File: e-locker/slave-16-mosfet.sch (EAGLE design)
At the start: 133 parts, among them IC1 PCF8574P, IC2 PCF8574P, IC3 PCF8574P, IC4 PCF8574P, Q1 BC547B, Q2 BC547B, Q3 BC547B, Q4 BC547B, Q5 BC547B, Q6 BC547B, Q7 BC547B, Q8 BC547B, T1 BC547, T2 BC547, T3 BC547, T4 BC547, T5 BC547, T6 BC547, T7 BC547, T8 BC547, X1 JST-XH-02-PIN-LONG-PAD, X10 JST-XH-04-PIN-LONG-PAD, X11 JST-XH-02-PIN-LONG-PAD, X12 JST-XH-04-PIN-LONG-PAD, X13 JST-XH-04-PIN-LONG-PAD, X14 JST-XH-04-PIN-LONG-PAD, X15 JST-XH-04-PIN-LONG-PAD, X16 JST-XH-04-PIN-LONG-PAD, X17 JST-XH-04-PIN-LONG-PAD, X18 JST-XH-04-PIN-LONG-PAD, X19 JST-XH-04-PIN-LONG-PAD, X2 JST-XH-05-PIN-LONG-PAD, X20 JST-XH-05-PIN-LONG-PAD, X21 JST-XH-02-PIN-LONG-PAD, X22 JST-XH-02-PIN-LONG-PAD, X3 JST-XH-04-PIN-LONG-PAD, X4 JST-XH-04-PIN-LONG-PAD, X5 JST-XH-04-PIN-LONG-PAD, X6 JST-XH-04-PIN-LONG-PAD, X7 JST-XH-04-PIN-LONG-PAD, X8 JST-XH-04-PIN-LONG-PAD, X9 JST-XH-04-PIN-LONG-PAD

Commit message: WIP
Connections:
- removed net N$11: R43.1, U$1.G
- new net N$81: R43.1, R59.2, U$1.G
- net N$12: now also R60.2
- net N$13: now also R61.2
- net N$14: now also R62.2
- net N$56: now also R66.2
- net N$59: now also R65.2
- net N$63: now also R64.2
- net N$64: now also R63.2
- net V24: no longer R59.2, R60.2, R61.2, R62.2, R63.2, R64.2, R65.2, R66.2
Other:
- moved on the sheet: R60, R61, R62, R63, R64, R65, R66

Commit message: new master and slave16 changes
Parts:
- removed JP2: (no value), pinhead-zmiany-JP:PINHD-2X8
- added JP3: (no value), adafruit:PINHD-2X4
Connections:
- net GND: now also JP3.2, JP3.4, JP3.6, JP3.8; no longer JP2.10, JP2.12, JP2.14, JP2.16, JP2.2, JP2.4, JP2.6, JP2.8
- net N$10: no longer JP2.15
- net N$17: no longer JP2.13
- net N$20: no longer JP2.11
- net N$21: no longer JP2.9
- net N$22: now also JP3.7; no longer JP2.7
- net N$23: now also JP3.5; no longer JP2.5
- net N$24: now also JP3.3; no longer JP2.3
- net N$25: now also JP3.1; no longer JP2.1
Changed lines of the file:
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@@
 <part name="X11" library="Rembrandt Electronics - JST XH Connectors v1-0" deviceset="JST-XH-02-PIN" device="-LONG-PAD"/>
 <part name="U$10" library="zort-library" deviceset="RS485-TTL-CONVERTER" device=""/>
-<part name="JP2" library="pinhead-zmiany-JP" deviceset="PINHD-2X8" device="" package3d_urn="urn:adsk.eagle:package:22481/2"/>
 <part name="IC1" library="micro-philips" library_urn="urn:adsk.eagle:library:290" deviceset="PCF8574" device="P" package3d_urn="urn:adsk.eagle:package:20171/1"/>
 <part name="IC2" library="micro-philips" library_urn="urn:adsk.eagle:library:290" deviceset="PCF8574" device="P" package3d_urn="urn:adsk.eagle:package:20171/1"/>
@@
 <part name="R65" library="eagle-ltspice" library_urn="urn:adsk.eagle:library:217" deviceset="R" device="R1206" package3d_urn="urn:adsk.eagle:package:13301/1"/>
 <part name="R66" library="eagle-ltspice" library_urn="urn:adsk.eagle:library:217" deviceset="R" device="R1206" package3d_urn="urn:adsk.eagle:package:13301/1"/>
+<part name="JP3" library="adafruit" library_urn="urn:adsk.eagle:library:420" deviceset="PINHD-2X4" device="" package3d_urn="urn:adsk.eagle:package:6240893/1"/>
 </parts>
 <sheets>
@@
 <attribute name="VALUE" x="205.74" y="91.44" size="1.778" layer="96"/>
 </instance>
-<instance part="JP2" gate="A" x="251.46" y="170.18" smashed="yes">
-<attribute name="NAME" x="245.11" y="180.975" size="1.778" layer="95"/>
-<attribute name="VALUE" x="245.11" y="154.94" size="1.778" layer="96"/>
-</instance>
 <instance part="IC1" gate="G$1" x="289.56" y="259.08" smashed="yes">
 <attribute name="NAME" x="281.94" y="275.59" size="1.778" layer="95"/>
@@
 <attribute name="NAME" x="361.95" y="146.2786" size="1.778" layer="95"/>
 <attribute name="VALUE" x="361.95" y="141.478" size="1.778" layer="96"/>
+</instance>
+<instance part="JP3" gate="A" x="251.46" y="172.72" smashed="yes">
+<attribute name="NAME" x="245.11" y="180.975" size="1.778" layer="95"/>
+<attribute name="VALUE" x="245.11" y="165.1" size="1.778" layer="96"/>
 </instance>
 </instances>
@@
 </segment>
 <segment>
-<pinref part="JP2" gate="A" pin="2"/>
 <wire x1="256.54" y1="177.8" x2="264.16" y2="177.8" width="0.1524" layer="91"/>
 <pinref part="GND3" gate="1" pin="GND"/>
 <wire x1="264.16" y1="177.8" x2="264.16" y2="175.26" width="0.1524" layer="91"/>
-<pinref part="JP2" gate="A" pin="4"/>
 <wire x1="264.16" y1="175.26" x2="264.16" y2="172.72" width="0.1524" layer="91"/>
 <wire x1="264.16" y1="172.72" x2="264.16" y2="170.18" width="0.1524" layer="91"/>
@@
 <wire x1="256.54" y1="175.26" x2="264.16" y2="175.26" width="0.1524" layer="91"/>
 <junction x="264.16" y="175.26"/>
-<pinref part="JP2" gate="A" pin="6"/>
 <wire x1="256.54" y1="172.72" x2="264.16" y2="172.72" width="0.1524" layer="91"/>
 <junction x="264.16" y="172.72"/>
-<pinref part="JP2" gate="A" pin="8"/>
 <wire x1="256.54" y1="170.18" x2="264.16" y2="170.18" width="0.1524" layer="91"/>
 <junction x="264.16" y="170.18"/>
-<pinref part="JP2" gate="A" pin="10"/>
 <wire x1="256.54" y1="167.64" x2="264.16" y2="167.64" width="0.1524" layer="91"/>
 <junction x="264.16" y="167.64"/>
-<pinref part="JP2" gate="A" pin="12"/>
 <wire x1="256.54" y1="165.1" x2="264.16" y2="165.1" width="0.1524" layer="91"/>
 <junction x="264.16" y="165.1"/>
-<pinref part="JP2" gate="A" pin="14"/>
 <wire x1="256.54" y1="162.56" x2="264.16" y2="162.56" width="0.1524" layer="91"/>
 <junction x="264.16" y="162.56"/>
-<pinref part="JP2" gate="A" pin="16"/>
 <wire x1="256.54" y1="160.02" x2="264.16" y2="160.02" width="0.1524" layer="91"/>
 <junction x="264.16" y="160.02"/>
@@
 <wire x1="243.84" y1="157.48" x2="264.16" y2="157.48" width="0.1524" layer="91"/>
 <junction x="264.16" y="157.48"/>
+<pinref part="JP3" gate="A" pin="2"/>
+<pinref part="JP3" gate="A" pin="4"/>
+<pinref part="JP3" gate="A" pin="6"/>
+<pinref part="JP3" gate="A" pin="8"/>
 </segment>
 <segment>
@@
 <net name="N$10" class="0">
 <segment>
-<pinref part="JP2" gate="A" pin="15"/>
 <wire x1="241.3" y1="160.02" x2="243.84" y2="160.02" width="0.1524" layer="91"/>
 <pinref part="U$20" gate="G$1" pin="D2"/>
@@
 <net name="N$17" class="0">
 <segment>
-<pinref part="JP2" gate="A" pin="13"/>
 <wire x1="241.3" y1="162.56" x2="243.84" y2="162.56" width="0.1524" layer="91"/>
 <pinref part="U$20" gate="G$1" pin="D3"/>
@@
 <net name="N$20" class="0">
 <segment>
-<pinref part="JP2" gate="A" pin="11"/>
 <wire x1="241.3" y1="165.1" x2="243.84" y2="165.1" width="0.1524" layer="91"/>
 <pinref part="U$20" gate="G$1" pin="D4"/>
@@
 <net name="N$21" class="0">
 <segment>
-<pinref part="JP2" gate="A" pin="9"/>
 <wire x1="241.3" y1="167.64" x2="243.84" y2="167.64" width="0.1524" layer="91"/>
 <pinref part="U$20" gate="G$1" pin="D5"/>
@@
 <net name="N$22" class="0">
 <segment>
-<pinref part="JP2" gate="A" pin="7"/>
 <wire x1="241.3" y1="170.18" x2="243.84" y2="170.18" width="0.1524" layer="91"/>
 <pinref part="U$20" gate="G$1" pin="D6"/>
 <wire x1="243.84" y1="170.18" x2="248.92" y2="170.18" width="0.1524" layer="91"/>
 <junction x="243.84" y="170.18"/>
+<pinref part="JP3" gate="A" pin="7"/>
 </segment>
 </net>
 <net name="N$23" class="0">
 <segment>
-<pinref part="JP2" gate="A" pin="5"/>
 <wire x1="241.3" y1="172.72" x2="243.84" y2="172.72" width="0.1524" layer="91"/>
 <pinref part="U$20" gate="G$1" pin="D7"/>
 <wire x1="243.84" y1="172.72" x2="248.92" y2="172.72" width="0.1524" layer="91"/>
 <junction x="243.84" y="172.72"/>
+<pinref part="JP3" gate="A" pin="5"/>
 </segment>
 </net>
 <net name="N$24" class="0">
 <segment>
-<pinref part="JP2" gate="A" pin="3"/>
 <wire x1="241.3" y1="175.26" x2="243.84" y2="175.26" width="0.1524" layer="91"/>
 <pinref part="U$20" gate="G$1" pin="D8"/>
 <wire x1="243.84" y1="175.26" x2="248.92" y2="175.26" width="0.1524" layer="91"/>
 <junction x="243.84" y="175.26"/>
+<pinref part="JP3" gate="A" pin="3"/>
 </segment>
 </net>
 <net name="N$25" class="0">
 <segment>
-<pinref part="JP2" gate="A" pin="1"/>
 <wire x1="241.3" y1="177.8" x2="243.84" y2="177.8" width="0.1524" layer="91"/>
 <pinref part="U$20" gate="G$1" pin="D9"/>
 <wire x1="243.84" y1="177.8" x2="248.92" y2="177.8" width="0.1524" layer="91"/>
 <junction x="243.84" y="177.8"/>
-</segment>
-</net>
+<pinref part="JP3" gate="A" pin="1"/>
+</segment>
+</net>

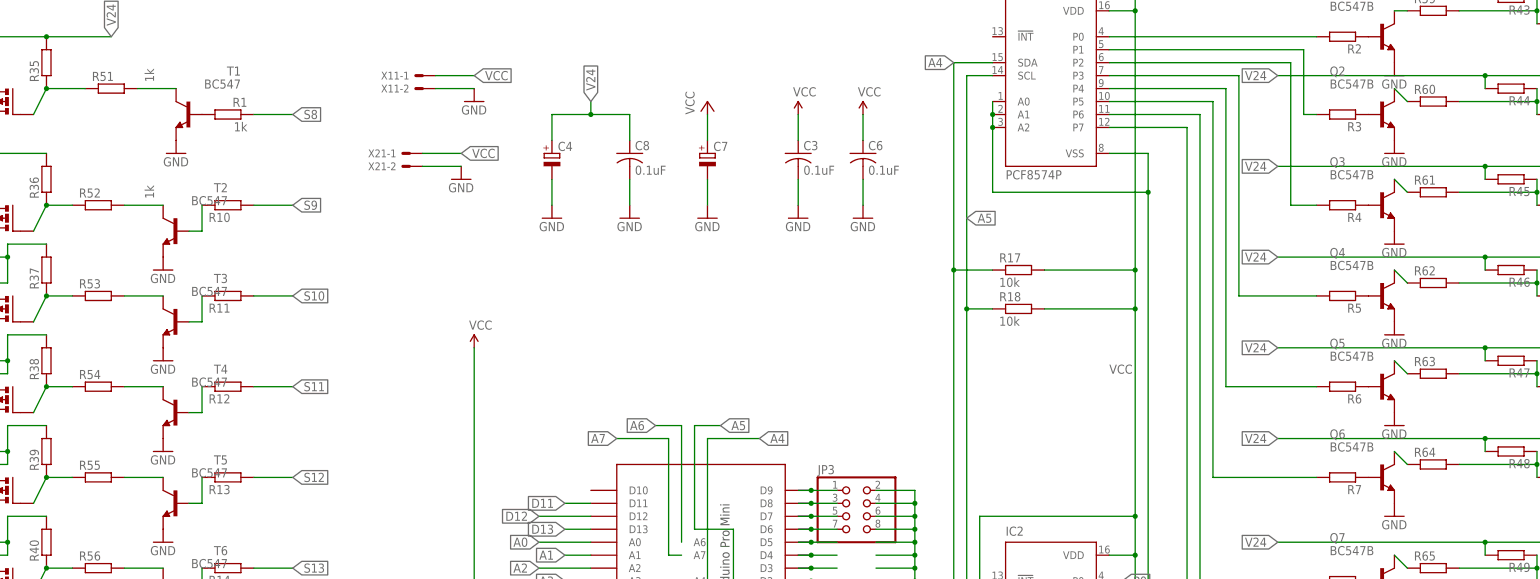
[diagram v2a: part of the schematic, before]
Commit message: mosfet slave fix
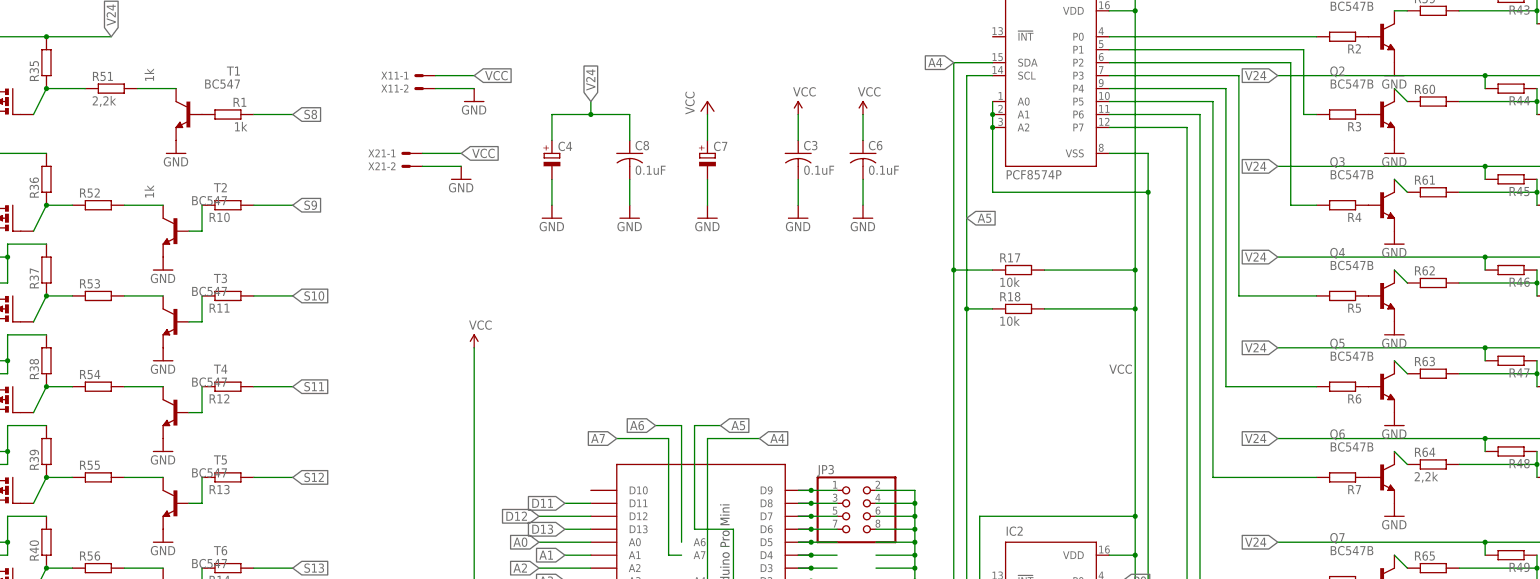
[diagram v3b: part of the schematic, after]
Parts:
- R51, R64: value (none) -> 2,2k
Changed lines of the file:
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@@
 <part name="Q7" library="transistor-npn" library_urn="urn:adsk.eagle:library:398" deviceset="BC547*" device="" package3d_urn="urn:adsk.eagle:package:28523/2" technology="B"/>
 <part name="Q8" library="transistor-npn" library_urn="urn:adsk.eagle:library:398" deviceset="BC547*" device="" package3d_urn="urn:adsk.eagle:package:28523/2" technology="B"/>
-<part name="R51" library="eagle-ltspice" library_urn="urn:adsk.eagle:library:217" deviceset="R" device="R1206" package3d_urn="urn:adsk.eagle:package:13301/1"/>
+<part name="R51" library="eagle-ltspice" library_urn="urn:adsk.eagle:library:217" deviceset="R" device="R1206" package3d_urn="urn:adsk.eagle:package:13301/1" value="2,2k"/>
 <part name="R52" library="eagle-ltspice" library_urn="urn:adsk.eagle:library:217" deviceset="R" device="R1206" package3d_urn="urn:adsk.eagle:package:13301/1"/>
 <part name="R53" library="eagle-ltspice" library_urn="urn:adsk.eagle:library:217" deviceset="R" device="R1206" package3d_urn="urn:adsk.eagle:package:13301/1"/>
@@
 <part name="R62" library="eagle-ltspice" library_urn="urn:adsk.eagle:library:217" deviceset="R" device="R1206" package3d_urn="urn:adsk.eagle:package:13301/1"/>
 <part name="R63" library="eagle-ltspice" library_urn="urn:adsk.eagle:library:217" deviceset="R" device="R1206" package3d_urn="urn:adsk.eagle:package:13301/1"/>
-<part name="R64" library="eagle-ltspice" library_urn="urn:adsk.eagle:library:217" deviceset="R" device="R1206" package3d_urn="urn:adsk.eagle:package:13301/1"/>
+<part name="R64" library="eagle-ltspice" library_urn="urn:adsk.eagle:library:217" deviceset="R" device="R1206" package3d_urn="urn:adsk.eagle:package:13301/1" value="2,2k"/>
 <part name="R65" library="eagle-ltspice" library_urn="urn:adsk.eagle:library:217" deviceset="R" device="R1206" package3d_urn="urn:adsk.eagle:package:13301/1"/>
 <part name="R66" library="eagle-ltspice" library_urn="urn:adsk.eagle:library:217" deviceset="R" device="R1206" package3d_urn="urn:adsk.eagle:package:13301/1"/>
